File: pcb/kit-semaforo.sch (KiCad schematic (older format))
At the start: 12 parts, among them P1 CONN_02X04

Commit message: v0.2a
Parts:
- BZ1: footprint Buzzers_Beepers:BUZZER -> Buzzers_Beepers:Buzzer_12x9.5RM7.6
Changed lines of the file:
@@
 F 0 "BZ1" H 4550 2550 50  0000 L CNN
 F 1 "Buzzer" H 4550 2450 50  0000 L CNN
-F 2 "Buzzers_Beepers:BUZZER" V 4375 2600 50  0001 C CNN
+F 2 "Buzzers_Beepers:Buzzer_12x9.5RM7.6" V 4375 2600 50  0001 C CNN
 F 3 "" V 4375 2600 50  0000 C CNN
 	1    4400 2500

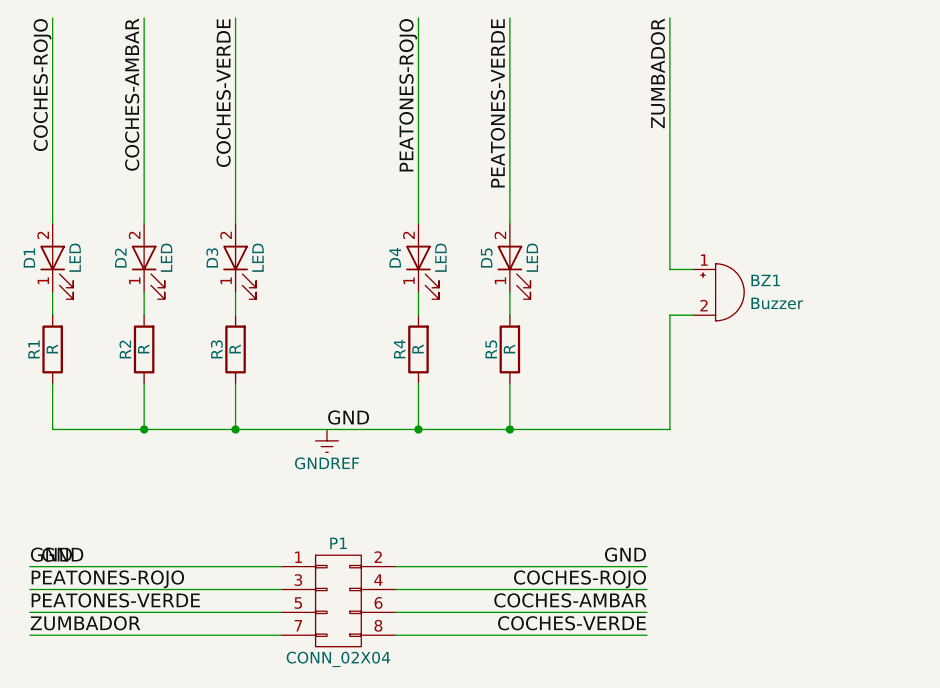
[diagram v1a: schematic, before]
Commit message: 0.3a Añadido botón para peatones
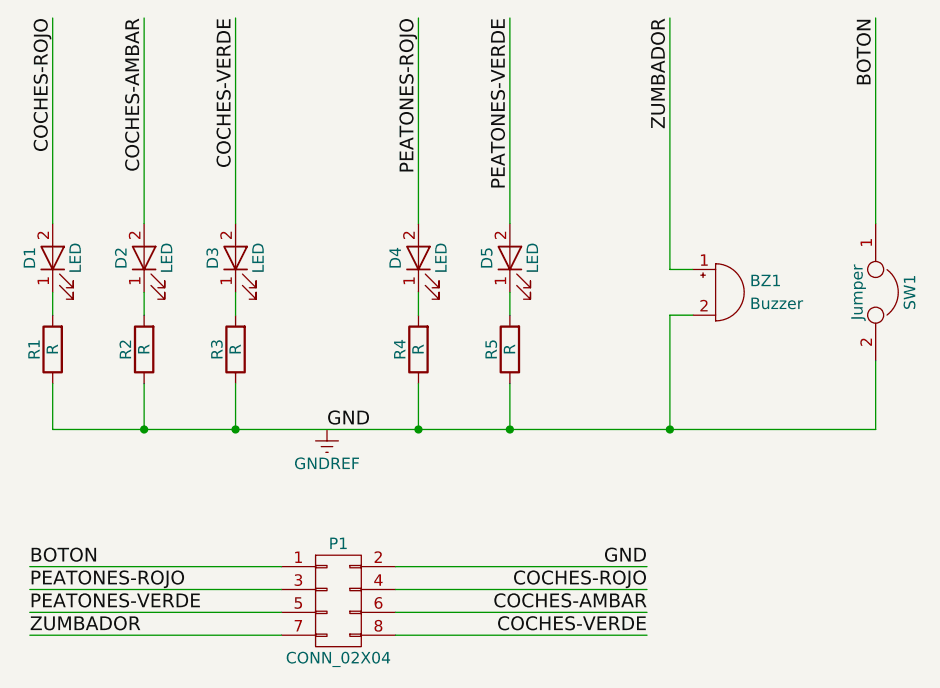
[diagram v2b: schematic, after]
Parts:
- added SW1: Jumper, Buttons_Switches_THT:SW_PUSH_6mm, symbol Jumper
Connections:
- net GNDREF: now also SW1.2; no longer P1.1 (P1)
- new net BOTON: P1.1 (P1), SW1.1
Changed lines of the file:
@@
 	1500 2900 1500 3100
 Wire Wire Line
-	1500 3100 4200 3100
+	1500 3100 5100 3100
 Wire Wire Line
 	3500 3100 3500 2900
@@
 Text Label 4100 3800 2    60   ~ 0
 COCHES-ROJO
-Text Label 1450 3700 0    60   ~ 0
+Text Label 4100 3700 2    60   ~ 0
 GND
 Text Label 1400 3700 0    60   ~ 0
-GND
-Text Label 4100 3700 2    60   ~ 0
-GND
+BOTON
+$Comp
+L Jumper SW1
+U 1 1 59328FB2
+P 5100 2500
+F 0 "SW1" H 5100 2650 50  0000 C CNN
+F 1 "Jumper" H 5100 2420 50  0000 C CNN
+F 2 "Buttons_Switches_THT:SW_PUSH_6mm" H 5100 2500 50  0001 C CNN
+F 3 "" H 5100 2500 50  0001 C CNN
+	1    5100 2500
+	0    1    1    0
+$EndComp
+Wire Wire Line
+	5100 2200 5100 1300
+Wire Wire Line
+	5100 3100 5100 2800
+Connection ~ 4200 3100
+Text Label 5100 1300 3    60   ~ 0
+BOTON
 $EndSCHEMATC
